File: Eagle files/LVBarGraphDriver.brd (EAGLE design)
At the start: 100 x 80 mm, 22 parts, among them IC1 74HC595D, IC2 74HC595D

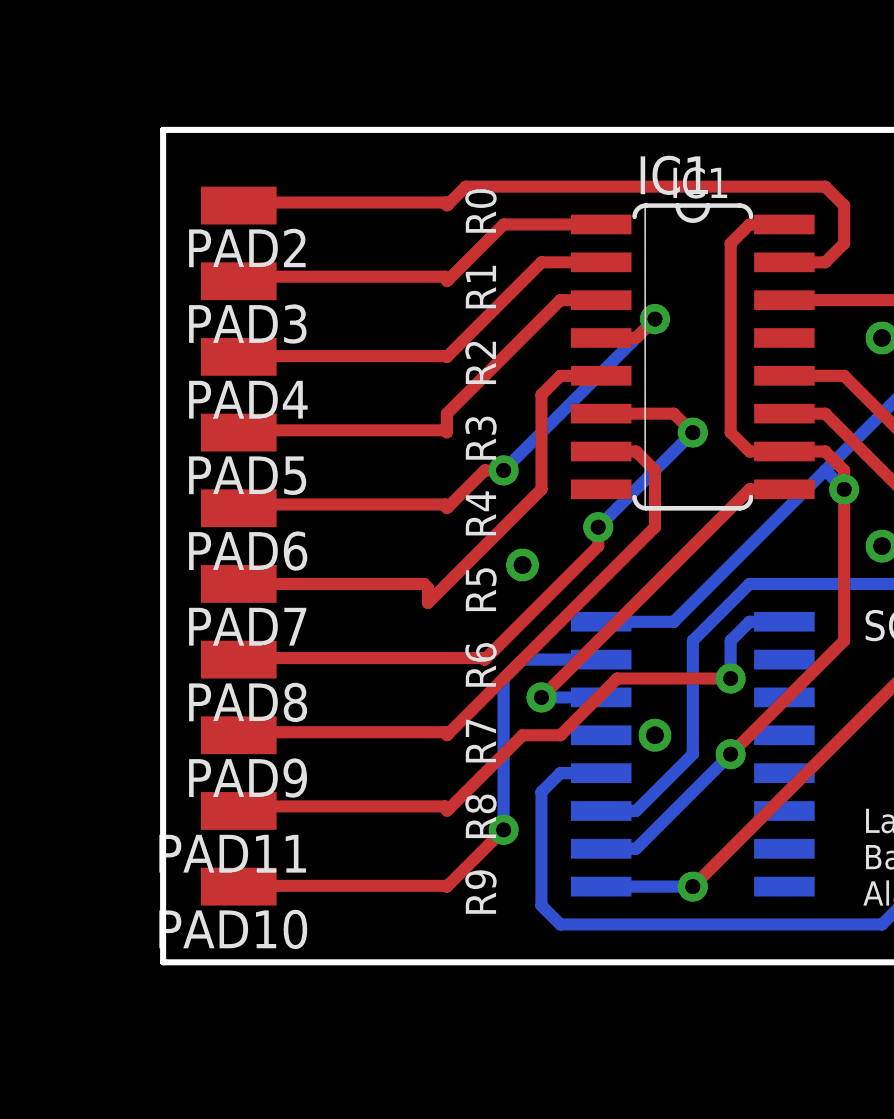
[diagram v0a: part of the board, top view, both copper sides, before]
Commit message: Prep for oshpark
Changed naming of BarGraphDriver to be more accurate, added a new bar
graph driver for non-lv boards, fixed the usb breakout to match our
standards and removed the text doc.
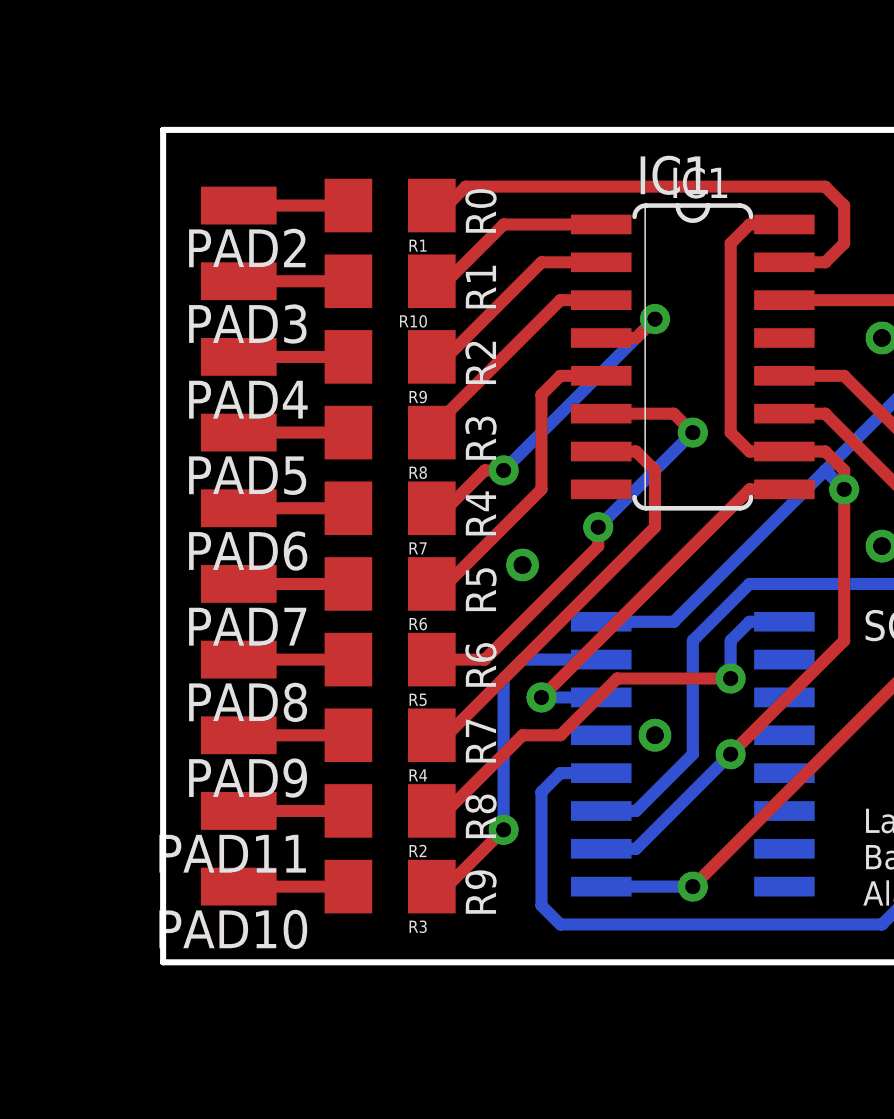
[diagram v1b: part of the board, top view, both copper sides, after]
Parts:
- added R1, R10, R2, R3, R4, R5, R6, R7, R8, R9: 68, SparkFun-Resistors:1206
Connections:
- new net N$1: PAD11.1, R2.2
- new net N$10: PAD2.1, R1.2
- new net N$2: PAD10.1, R3.2
- new net N$3: PAD9.1, R4.2
- new net N$4: PAD8.1, R5.2
- new net N$5: PAD7.1, R6.2
- new net N$6: PAD6.1, R7.2
- new net N$7: PAD5.1, R8.2
- new net N$8: PAD4.1, R9.2
- new net N$9: PAD3.1, R10.2
- net N$11: now also R1.1; no longer PAD2.1
- net N$12: now also R10.1; no longer PAD3.1
- net N$13: now also R9.1; no longer PAD4.1
- net N$14: now also R8.1; no longer PAD5.1
- net N$15: now also R7.1; no longer PAD6.1
- net N$16: now also R6.1; no longer PAD7.1
- net N$17: now also R5.1; no longer PAD8.1
- net N$18: now also R4.1; no longer PAD9.1
- net N$19: now also R3.1; no longer PAD10.1
- net N$20: now also R2.1; no longer PAD11.1
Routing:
- net N$12: track 13.2 -> 6.48 mm
- net N$20: track 21.9 -> 15.2 mm
- net N$15: track 18.9 -> 12.2 mm
- net N$11: track 24.5 -> 17.9 mm
- net N$18: track 21.0 -> 14.4 mm
- net N$14: track 14.5 -> 7.90 mm
- net N$17: track 22.2 -> 15.6 mm
- net N$19: track 18.3 -> 11.8 mm
- net N$13: track 13.5 -> 7.00 mm
- net N$16: track 17.7 -> 11.5 mm
- net N$9: track 0.00 -> 3.68 mm
- net N$8: track 0.00 -> 3.68 mm
- net N$7: track 0.00 -> 3.68 mm
- net N$6: track 0.00 -> 3.68 mm
- net N$5: track 0.00 -> 3.68 mm
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
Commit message: Fixes
Removed outer footprint of board so that each board is now the correct
size instead of that of the default footprint.
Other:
- board size 100 x 80 mm -> 33 x 27.9 mm
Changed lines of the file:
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@@
 <board>
 <plain>
-<wire x1="0" y1="0" x2="100" y2="0" width="0" layer="20"/>
-<wire x1="100" y1="0" x2="100" y2="80" width="0" layer="20"/>
-<wire x1="100" y1="80" x2="0" y2="80" width="0" layer="20"/>
-<wire x1="0" y1="80" x2="0" y2="0" width="0" layer="20"/>
 <wire x1="15.24" y1="50.8" x2="15.24" y2="22.86" width="0.2032" layer="20"/>
 <wire x1="15.24" y1="22.86" x2="48.26" y2="22.86" width="0.2032" layer="20"/>

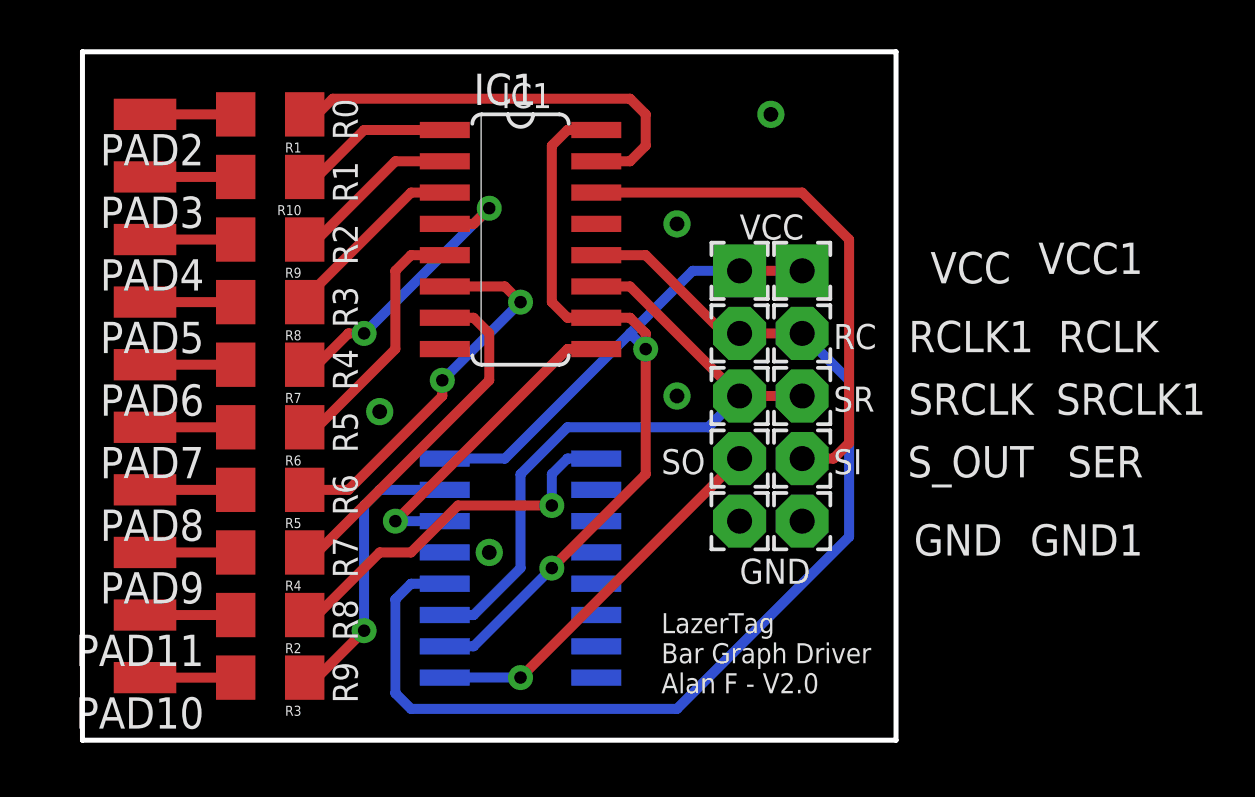
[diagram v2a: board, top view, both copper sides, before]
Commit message: aaaaaaaaaaaaaaaaaaaaaaaaaaaaaaaaaaaa
Cleaned up schematics, replaced wire solder points with header pin
mounts for standardization, recreated a broken file and dealt with the
confusion and insanity that followed.
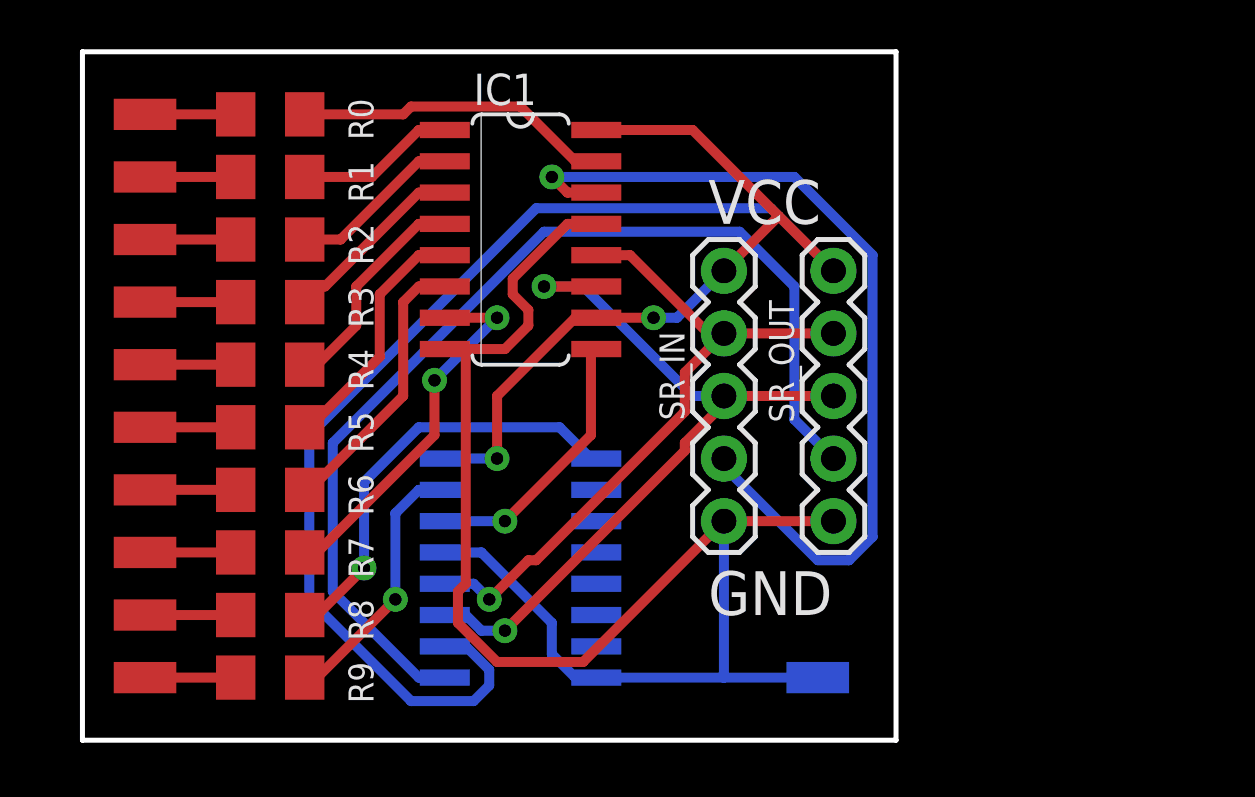
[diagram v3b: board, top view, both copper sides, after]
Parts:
- removed GND, GND1, RCLK, RCLK1, SER, SRCLK, SRCLK1, S_OUT: WIREPAD2,15/1,0, wirepad:2,15/1,0
- removed VCC, VCC1: WIREPAD2,15/1,0, smallWirepadSquare:2,15/1,0
- added PAD1: (no value), wirepad:SMD1,27-2,54
- added SR_IN, SR_OUT: (no value), SparkFun-Connectors:1X05
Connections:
- removed net SER: IC1.14, SER.1
- removed net SRCLK: IC1.11, IC2.11, SRCLK.1, SRCLK1.1
- removed net S_OUT: IC2.9, S_OUT.1
- new net SCLK: IC1.11, IC2.11, SR_IN.3, SR_OUT.3
- new net SER_IN: IC1.14, SR_IN.4
- new net SER_OUT: IC2.9, SR_OUT.4
- net GND: now also PAD1.1, SR_IN.5, SR_OUT.5; no longer GND.1, GND1.1
- net RCLK: now also SR_IN.2, SR_OUT.2; no longer RCLK.1, RCLK1.1
- net VCC: now also SR_IN.1, SR_OUT.1; no longer VCC.1, VCC1.1
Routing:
- net GND: track 0.00 -> 64.1 mm, vias 4 -> 0
- net SER_OUT: track 0.00 -> 42.9 mm
- net SER_IN: track 0.00 -> 36.2 mm, vias 0 -> 1
- net SCLK: track 0.00 -> 31.6 mm, vias 0 -> 2
- net SRCLK: track 28.1 -> 0.00 mm
- net VCC: track 48.1 -> 76.0 mm
- net SER: track 21.5 -> 0.00 mm
- net RCLK: track 46.4 -> 27.7 mm, vias 0 -> 1
- net S_OUT: track 15.6 -> 0.00 mm, vias 1 -> 0
- net N$11: track 17.9 -> 12.9 mm
- net N$17: track 15.6 -> 11.3 mm, vias 2 -> 0
- net N$15: track 12.2 -> 8.98 mm, vias 2 -> 0
- net N$20: track 15.2 -> 17.6 mm
- net N$22: track 13.1 -> 11.1 mm
- net N$19: track 11.8 -> 10.9 mm
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- removed copper zone on layer 1, net GND
- removed copper zone on layer 16, net GND
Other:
- board text added: "LazerTag Bar Graph Driver Alan F - V2.1 Greg T. (mod)"
- board text removed: "IC1"
- board text removed: "IC2"
- board text removed: "LazerTag Bar Graph Driver Alan F - V2.0"
- board text removed: "RC"
- board text removed: "SI"
- board text removed: "SO"
- board text removed: "SR"

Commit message: Fixes
more fixes >:|
should e ready for fabbing
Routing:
- added copper zone on layer 1, net GND
- added copper zone on layer 16, net GND
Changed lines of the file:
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@@
 <?xml version="1.0" encoding="utf-8"?>
 <!DOCTYPE eagle SYSTEM "eagle.dtd">
-<eagle version="7.5.0">
+<eagle version="7.4.0">
 <drawing>
 <settings>
@@
 <wire x1="41.275" y1="31.75" x2="35.56" y2="26.035" width="0.4064" layer="1"/>
 <wire x1="30.7975" y1="38.735" x2="29.9466" y2="38.735" width="0.4064" layer="1"/>
+<polygon width="0.4064" layer="1">
+<vertex x="15.24" y="50.8"/>
+<vertex x="48.26" y="50.8"/>
+<vertex x="48.26" y="22.86"/>
+<vertex x="15.24" y="22.86"/>
+</polygon>
+<polygon width="0.4064" layer="16">
+<vertex x="15.24" y="50.8"/>
+<vertex x="48.26" y="50.8"/>
+<vertex x="48.26" y="22.86"/>
+<vertex x="15.24" y="22.86"/>
+</polygon>
 </signal>
 <signal name="VCC" class="1">
@@
 <wire x1="28.8925" y1="45.085" x2="25.0825" y2="41.275" width="0.4064" layer="1"/>
 <wire x1="29.9466" y1="45.085" x2="28.8925" y2="45.085" width="0.4064" layer="1"/>
-<wire x1="24.765" y1="41.275" x2="24.26" y2="40.64" width="0" layer="19" extent="1-16"/>
 </signal>
 <signal name="N$15" class="2">
